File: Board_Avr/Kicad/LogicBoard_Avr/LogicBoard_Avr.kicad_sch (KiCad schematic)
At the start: 11 parts, among them SW1 Reset switch, U1 ATmega328PB-A

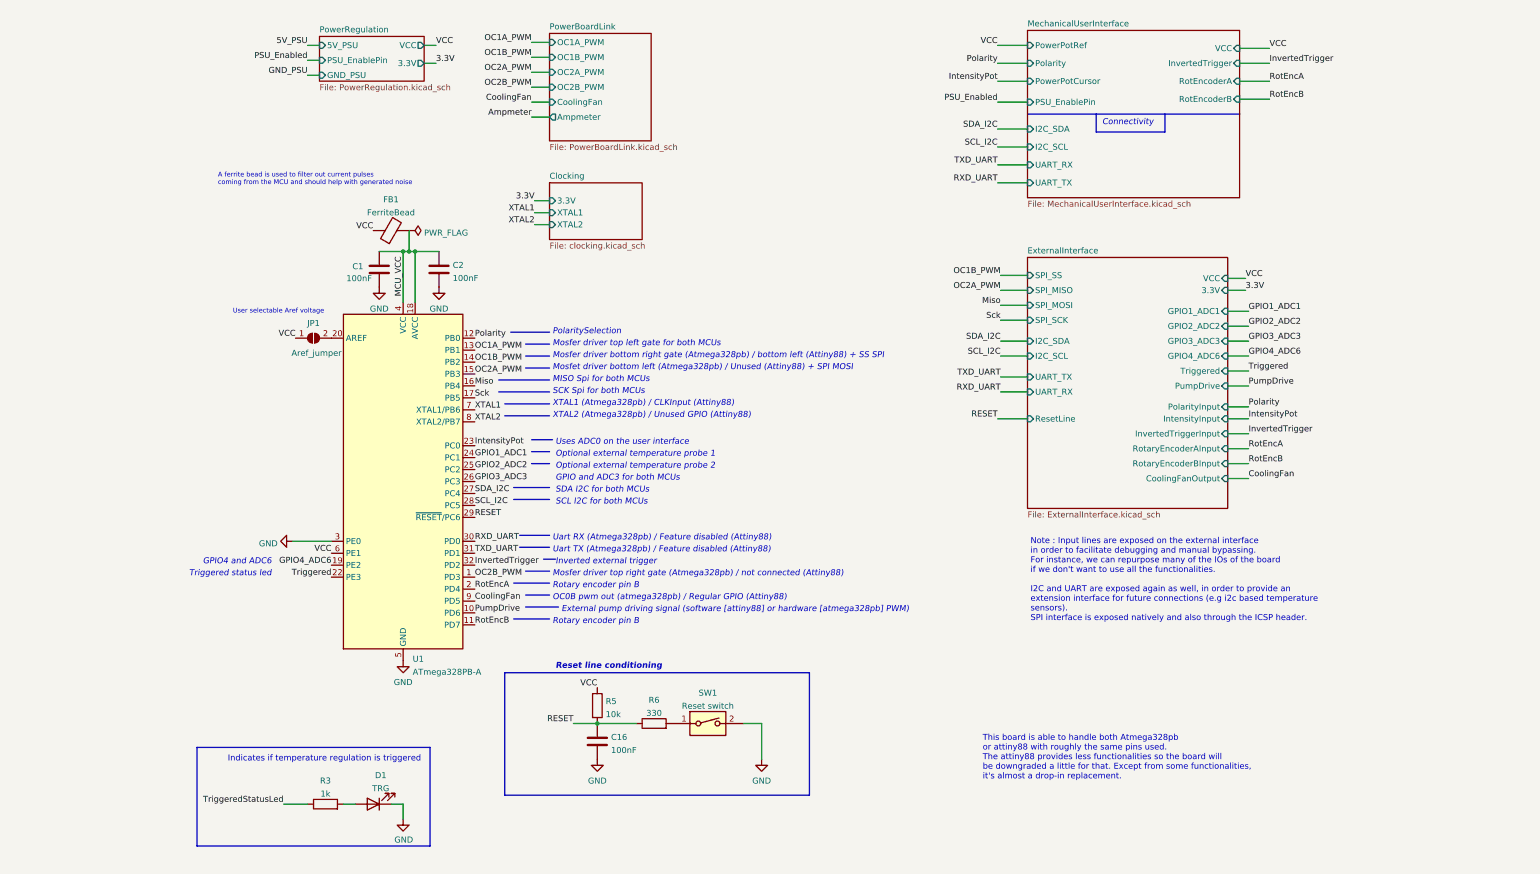
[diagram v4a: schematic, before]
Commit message: Fixed misorganised pins and updated pin mapping table
Signed-off-by: bebenlebricolo <benoittarrade@hotmail.fr>
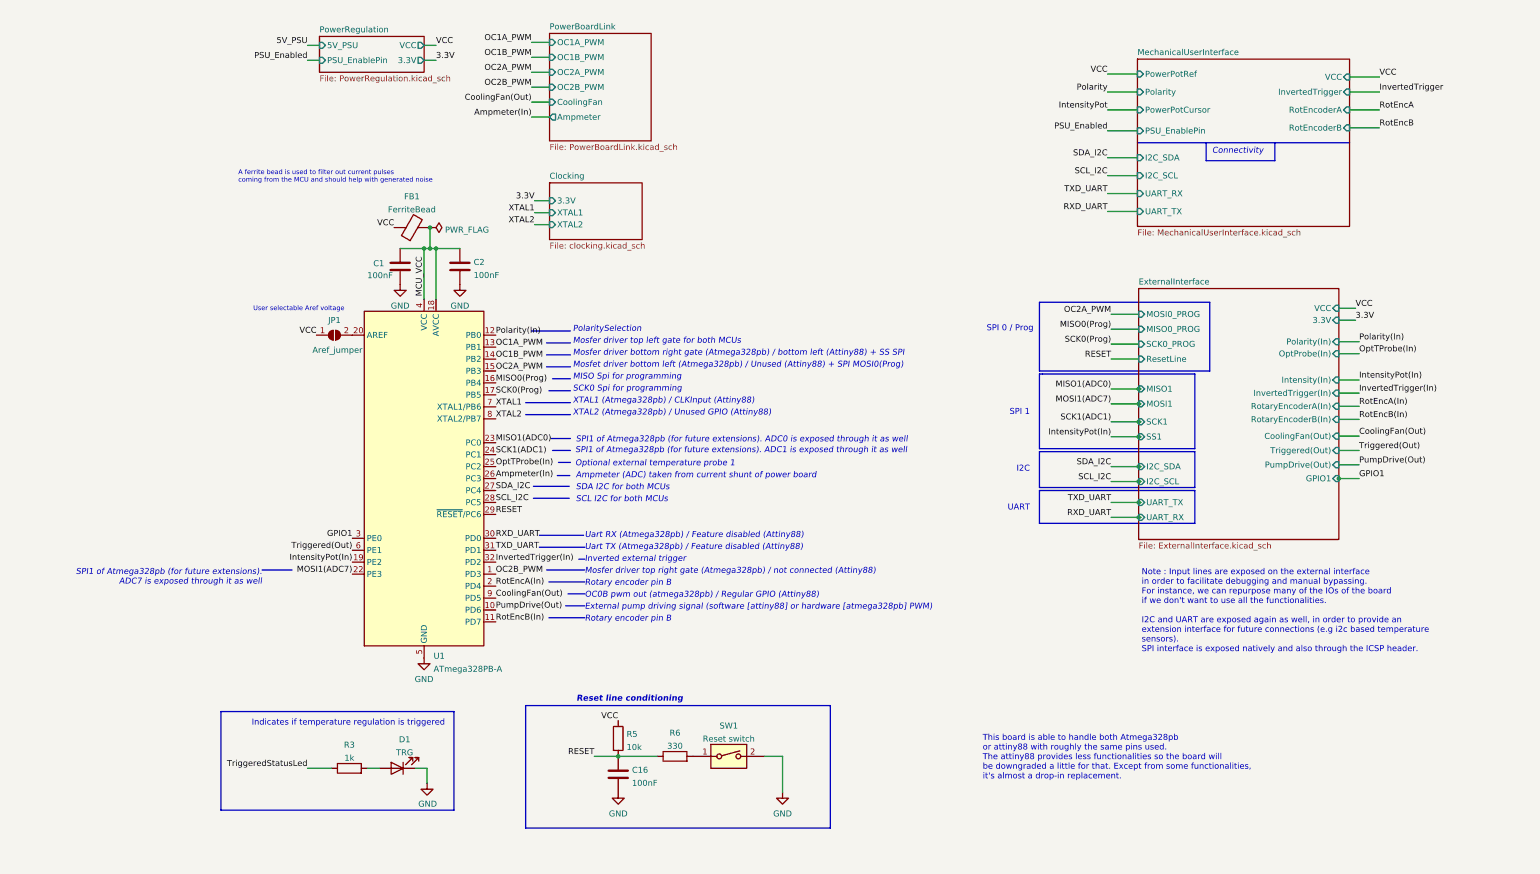
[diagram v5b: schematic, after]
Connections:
- net GND: no longer U1.3 (PE0)
- net IntensityPot: no longer U1.23 (PC0)
- net InvertedTrigger: no longer U1.32 (PD2)
- net Polarity: no longer U1.12 (PB0)
- net RotEncA: no longer U1.2 (PD4)
- net RotEncB: no longer U1.11 (PD7)
- net VCC: no longer U1.6 (PE1)
- net CoolingFan renamed CoolingFan(Out)
- net GPIO1_ADC1 renamed SCK1(ADC1)
- net GPIO2_ADC2 renamed OptTProbe(In)
- net GPIO3_ADC3 renamed Ampmeter(In)
- net GPIO4_ADC6 renamed IntensityPot(In)
- net Miso renamed MISO0(Prog)
- net PumpDrive renamed PumpDrive(Out)
- net Sck renamed SCK0(Prog)
- net Triggered renamed MOSI1(ADC7)
- new net GPIO1: U1.3 (PE0)
- new net InvertedTrigger(In): U1.32 (PD2)
- new net MISO1(ADC0): U1.23 (PC0)
- new net Polarity(In): U1.12 (PB0)
- new net RotEncA(In): U1.2 (PD4)
- new net RotEncB(In): U1.11 (PD7)
- new net Triggered(Out): U1.6 (PE1)
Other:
- sheet ExternalInterface ports: added CoolingFan(Out), GPIO1, Intensity(In), InvertedTrigger(In), MISO0_PROG, MISO1, MOSI0_PROG, MOSI1, OptProbe(In), Polarity(In), PumpDrive(Out), RotaryEncoderA(In), RotaryEncoderB(In), SCK0_PROG, SCK1, SS1, Triggered(Out); removed CoolingFanOutput, GPIO1_ADC1, GPIO2_ADC2, GPIO3_ADC3, GPIO4_ADC6, IntensityInput, InvertedTriggerInput, PolarityInput, PumpDrive, RotaryEncoderAInput, RotaryEncoderBInput, SPI_MISO, SPI_MOSI, SPI_SCK, SPI_SS, Triggered
- sheet PowerRegulation ports: added none; removed GND_PSU
- note added: "Ampmeter (ADC) taken from current shunt of power board"
- note added: "I2C"
- note added: "MISO Spi for programming"
- note added: "Mosfet driver bottom left (Atmega328pb) / Unused (Attiny88) + SPI MOSI0(Prog)"
- note added: "SCK0 Spi for programming"
- note added: "SPI 0 / Prog"
- note added: "SPI 1"
- note added: "SPI1 of Atmega328pb (for future extensions). ADC0 is exposed through it as well"
- note added: "SPI1 of Atmega328pb (for future extensions). ADC1 is exposed through it as well"
- note added: "SPI1 of Atmega328pb (for future extensions). ADC7 is exposed through it as well"
- note added: "UART"
- note removed: "GPIO and ADC3 for both MCUs"
- note removed: "GPIO4 and ADC6"
- note removed: "MISO Spi for both MCUs"
- note removed: "Mosfet driver bottom left (Atmega328pb) / Unused (Attiny88) + SPI MOSI"
- note removed: "Optional external temperature probe 2"
- note removed: "SCK Spi for both MCUs"
- note removed: "Triggered status led"
- note removed: "Uses ADC0 on the user interface"
- moved on the sheet: C1, C16, C2, D1, FB1, JP1, R3, R5, R6, SW1, U1

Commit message: Started routing all traces
Signed-off-by: bebenlebricolo <benoittarrade@hotmail.fr>
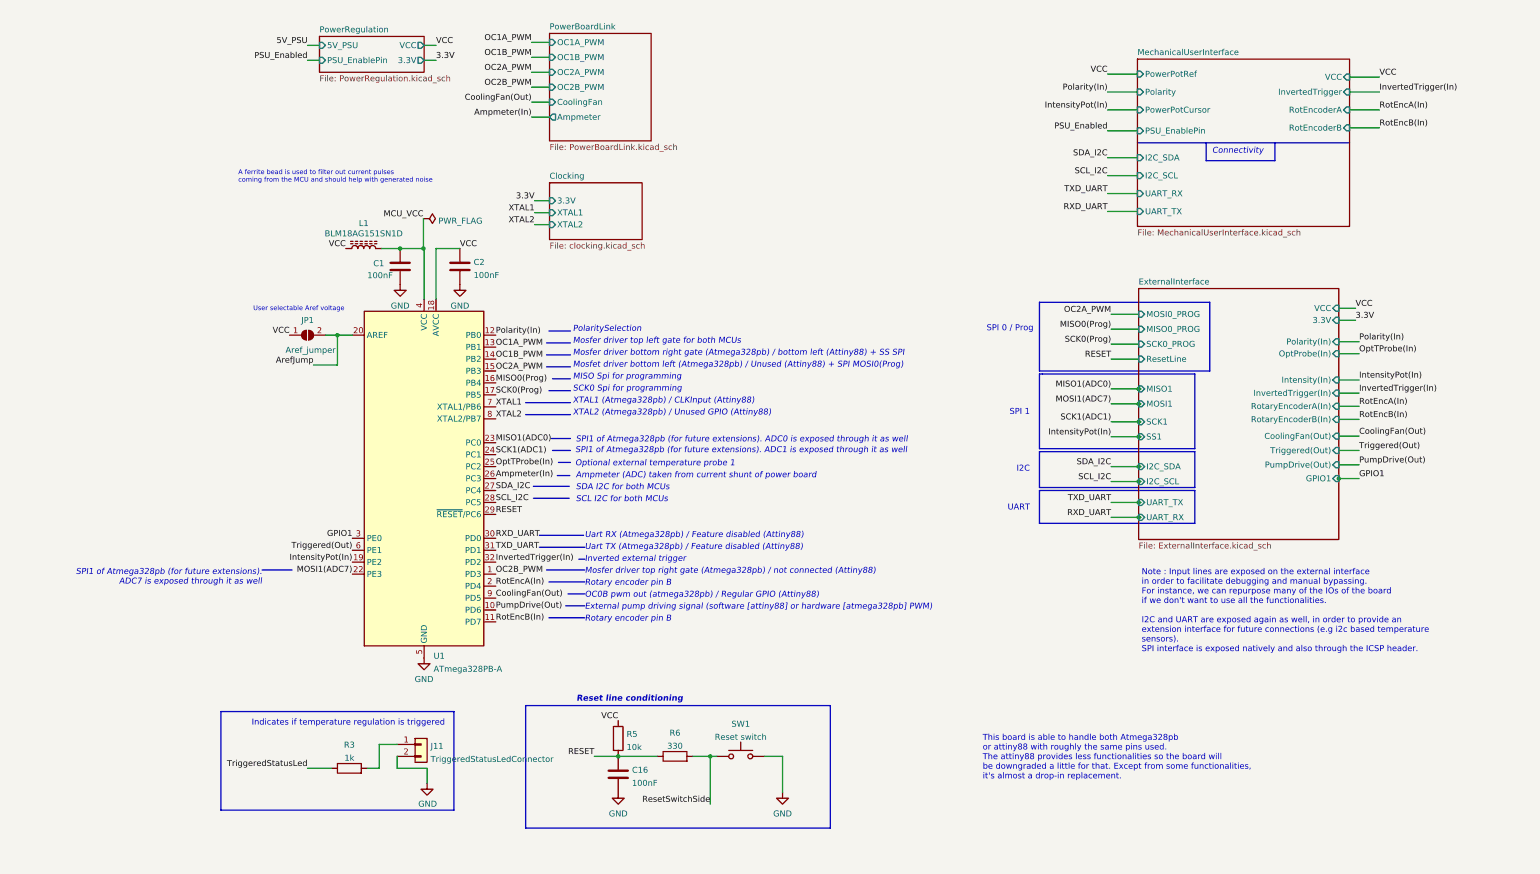
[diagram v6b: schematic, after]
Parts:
- removed D1: TRG, symbol Device:LED
- removed FB1: FerriteBead, symbol Device:FerriteBead
- removed SW1: Reset switch, symbol Switch:SW_DIP_x01
- added J11: TriggeredStatusLedConnector, Connector_PinHeader_2.54mm:PinHeader_1x02_P2.54mm_Vertical, symbol Connector_Generic:Conn_01x02
- added L1: BLM18AG151SN1D, Capacitor_SMD:C_0603_1608Metric, symbol Device:L_Ferrite
- added SW1: Reset switch, Button_Switch_THT:SW_PUSH_6mm_H4.3mm, symbol Switch:SW_Push
- C1, C16, C2: footprint (none) -> Capacitor_SMD:C_1206_3216Metric
- JP1: footprint (none) -> Jumper:SolderJumper-2_P1.3mm_Open_RoundedPad1.0x1.5mm
- R3, R5, R6: footprint (none) -> Resistor_SMD:R_1206_3216Metric_Pad1.30x1.75mm_HandSolder
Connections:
- net GND: now also J11.2 (Pin_2), SW1.2
- net MCU_VCC: now also L1.2; no longer C2.1, U1.18 (AVCC)
- net VCC: now also C2.1, U1.18 (AVCC), L1.1
- net at R3.2: now also J11.1 (Pin_1)
- net ArefJump: now reaches JP1.2 (B), U1.20 (AREF)
- net ResetSwitchSide: now reaches R6.2
- net ResetSwitchSide: now also SW1.1
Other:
- moved on the sheet: JP1

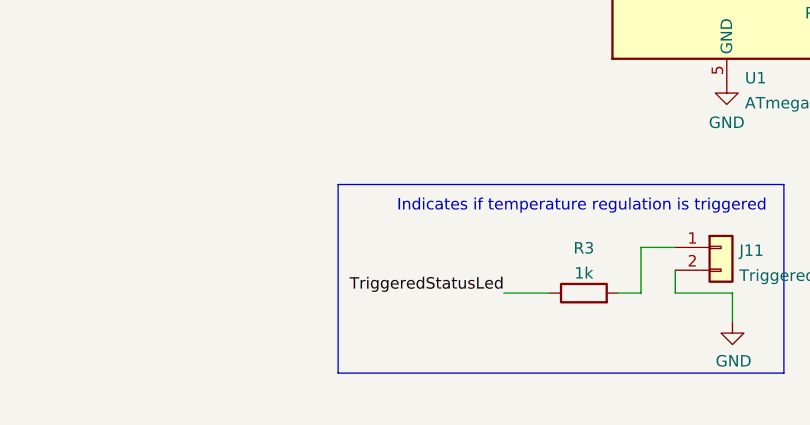
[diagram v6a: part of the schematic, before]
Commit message: Removed all microvias (unsupported by JLCPCB)
Signed-off-by: bebenlebricolo <benoittarrade@hotmail.fr>
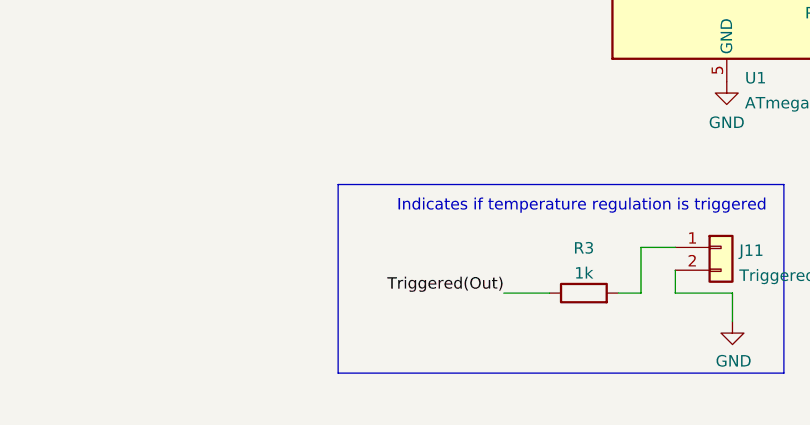
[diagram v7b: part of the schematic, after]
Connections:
- net TriggeredStatusLed is gone; now on net Triggered(Out): R3.1
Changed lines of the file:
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@@
     (effects (font (size 1.27 1.27)) (justify left bottom))
+  )
+  (label "Triggered(Out)" (at 36.83 175.26 180)
+    (effects (font (size 1.27 1.27)) (justify right bottom))
   )
   (label "Polarity(In)" (at 206.883 31.496 180)
@@
     (effects (font (size 1.27 1.27)) (justify left bottom))
   )
-  (label "TriggeredStatusLed" (at 36.83 175.26 180)
-    (effects (font (size 1.27 1.27)) (justify right bottom))
-  )
   (label "CoolingFan(Out)" (at 84.455 33.655 180)

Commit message: Finalised routing
Signed-off-by: bebenlebricolo <benoittarrade@hotmail.fr>
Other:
- sheet ExternalInterface ports: added none; removed I2C_SCL, I2C_SDA, UART_RX, UART_TX
- note removed: "I2C"
- note removed: "UART"
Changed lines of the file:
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@@
   (junction (at 122.428 172.72) (diameter 0) (color 0 0 0 0)
   )
-  (junction (at 213.487 111.125) (diameter 0) (color 0 0 0 0)
-  )
-  (junction (at 213.487 114.3) (diameter 0) (color 0 0 0 0)
-  )
   (junction (at 61.468 64.77) (diameter 0) (color 0 0 0 0)
   )
-  (junction (at 213.487 121.92) (diameter 0) (color 0 0 0 0)
-  )
   (junction (at 43.18 83.185) (diameter 0) (color 0 0 0 0)
   )
@@
   (junction (at 213.487 104.775) (diameter 0) (color 0 0 0 0)
   )
-  (junction (at 213.487 118.745) (diameter 0) (color 0 0 0 0)
-  )
   (junction (at 102.87 172.72) (diameter 0) (color 0 0 0 0)
   )
@@
     (stroke (width 0) (type default) (color 0 0 0 0))
   )
-  (polyline (pts (xy 192.405 107.95) (xy 225.425 107.95))
-    (stroke (width 0) (type default) (color 0 0 0 0))
-  )
   (wire (pts (xy 207.645 81.915) (xy 213.487 81.915))
     (stroke (width 0) (type default) (color 0 0 0 0))
@@
     (stroke (width 0) (type solid) (color 0 0 0 0))
   )
-  (wire (pts (xy 213.487 118.745) (xy 213.995 118.745))
-    (stroke (width 0) (type default) (color 0 0 0 0))
-  )
-  (wire (pts (xy 213.487 121.92) (xy 213.995 121.92))
-    (stroke (width 0) (type default) (color 0 0 0 0))
-  )
   (wire (pts (xy 256.032 107.696) (xy 260.35 107.696))
     (stroke (width 0) (type default) (color 0 0 0 0))
@@
     (stroke (width 0) (type default) (color 0 0 0 0))
   )
-  (polyline (pts (xy 225.425 115.57) (xy 192.405 115.57))
-    (stroke (width 0) (type default) (color 0 0 0 0))
-  )
   (polyline (pts (xy 242.443 46.101) (xy 242.443 42.291))
     (stroke (width 0) (type default) (color 0 0 0 0))
@@
     (stroke (width 0) (type default) (color 0 0 0 0))
   )
-  (polyline (pts (xy 192.405 107.95) (xy 192.405 115.57))
-    (stroke (width 0) (type default) (color 0 0 0 0))
-  )
   (wire (pts (xy 84.455 24.13) (xy 88.265 24.13))
     (stroke (width 0) (type default) (color 0 0 0 0))
@@
     (stroke (width 0) (type default) (color 0 0 0 0))
   )
-  (polyline (pts (xy 192.405 116.205) (xy 225.425 116.205))
-    (stroke (width 0) (type default) (color 0 0 0 0))
-  )
   (wire (pts (xy 207.645 104.775) (xy 213.487 104.775))
     (stroke (width 0) (type default) (color 0 0 0 0))
@@
     (stroke (width 0) (type default) (color 0 0 0 0))
   )
-  (polyline (pts (xy 192.405 116.205) (xy 192.405 123.19))
-    (stroke (width 0) (type default) (color 0 0 0 0))
-  )
   (wire (pts (xy 84.455 27.305) (xy 88.265 27.305))
     (stroke (width 0) (type default) (color 0 0 0 0))
@@
     (stroke (width 0) (type solid) (color 0 0 0 0))
   )
-  (wire (pts (xy 207.645 121.92) (xy 213.487 121.92))
-    (stroke (width 0) (type default) (color 0 0 0 0))
-  )
   (polyline (pts (xy 225.425 91.44) (xy 225.425 107.315))
     (stroke (width 0) (type default) (color 0 0 0 0))
@@
     (stroke (width 0) (type default) (color 0 0 0 0))
   )
-  (wire (pts (xy 207.645 118.745) (xy 213.487 118.745))
-    (stroke (width 0) (type default) (color 0 0 0 0))
-  )
   (wire (pts (xy 55.88 175.26) (xy 62.23 175.26))
     (stroke (width 0) (type default) (color 0 0 0 0))
@@
     (stroke (width 0) (type default) (color 0 0 0 0))
   )
-  (polyline (pts (xy 225.425 107.95) (xy 225.425 115.57))
-    (stroke (width 0) (type default) (color 0 0 0 0))
-  )
   (wire (pts (xy 213.233 56.896) (xy 206.883 56.896))
     (stroke (width 0) (type default) (color 0 0 0 0))
@@
     (stroke (width 0) (type default) (color 0 0 0 0))
   )
-  (wire (pts (xy 213.487 111.125) (xy 213.995 111.125))
-    (stroke (width 0) (type default) (color 0 0 0 0))
-  )
-  (polyline (pts (xy 225.425 123.19) (xy 192.405 123.19))
-    (stroke (width 0) (type default) (color 0 0 0 0))
-  )
-  (wire (pts (xy 213.487 114.3) (xy 213.995 114.3))
-    (stroke (width 0) (type default) (color 0 0 0 0))
-  )
   (wire (pts (xy 213.487 101.6) (xy 213.995 101.6))
     (stroke (width 0) (type default) (color 0 0 0 0))
@@
     (stroke (width 0) (type default) (color 0 0 0 0))
   )
-  (wire (pts (xy 207.645 111.125) (xy 213.487 111.125))
-    (stroke (width 0) (type default) (color 0 0 0 0))
-  )
   (wire (pts (xy 256.032 80.01) (xy 259.588 80.01))
     (stroke (width 0) (type default) (color 0 0 0 0))
@@
     (stroke (width 0) (type default) (color 0 0 0 0))
   )
-  (wire (pts (xy 207.645 114.3) (xy 213.487 114.3))
-    (stroke (width 0) (type default) (color 0 0 0 0))
-  )
   (wire (pts (xy 256.032 98.298) (xy 260.35 98.298))
     (stroke (width 0) (type default) (color 0 0 0 0))
@@
   )
   (wire (pts (xy 84.455 30.48) (xy 88.265 30.48))
-    (stroke (width 0) (type default) (color 0 0 0 0))
-  )
-  (polyline (pts (xy 225.425 116.205) (xy 225.425 123.19))
     (stroke (width 0) (type default) (color 0 0 0 0))
   )
@@
     (effects (font (size 1.27 1.27) italic) (justify right bottom))
   )
-  (text "UART" (at 190.373 120.65 180)
-    (effects (font (size 1.27 1.27)) (justify right bottom))
-  )
   (text "Rotary encoder pin B" (at 95.758 144.272 0)
     (effects (font (size 1.27 1.27) italic) (justify left bottom))
@@
   (text "Inverted external trigger " (at 95.758 131.572 0)
     (effects (font (size 1.27 1.27) italic) (justify left bottom))
-  )
-  (text "I2C " (at 190.373 112.395 180)
-    (effects (font (size 1.27 1.27)) (justify right bottom))
   )
   (text "Connectivity" (at 229.108 44.831 0)
@@
     (effects (font (size 1.27 1.27)) (justify left bottom))
   )
-  (label "TXD_UART" (at 207.645 118.745 180)
-    (effects (font (size 1.27 1.27)) (justify right bottom))
-  )
   (label "IntensityPot(In)" (at 207.645 104.775 180)
     (effects (font (size 1.27 1.27)) (justify right bottom))
@@
     (effects (font (size 1.27 1.27)) (justify right bottom))
   )
-  (label "RXD_UART" (at 207.645 121.92 180)
-    (effects (font (size 1.27 1.27)) (justify right bottom))
-  )
   (label "XTAL1" (at 85.09 57.15 180)
     (effects (font (size 1.27 1.27)) (justify right bottom))
@@
     (effects (font (size 1.27 1.27)) (justify right bottom))
   )
-  (label "SCL_I2C" (at 207.645 114.3 180)
-    (effects (font (size 1.27 1.27)) (justify right bottom))
-  )
   (label "OC2A_PWM" (at 207.645 78.74 180)
     (effects (font (size 1.27 1.27)) (justify right bottom))
@@
   (label "VCC" (at 264.668 28.321 0)
     (effects (font (size 1.27 1.27)) (justify left bottom))
-  )
-  (label "SDA_I2C" (at 207.645 111.125 180)
-    (effects (font (size 1.27 1.27)) (justify right bottom))
   )
   (label "SCK0(Prog)" (at 76.835 95.885 0)
@@
       (effects (font (size 1.27 1.27)) (justify left top))
     )
-    (pin "I2C_SDA" input (at 213.487 111.125 180)
-      (effects (font (size 1.27 1.27)) (justify left))
-    )
-    (pin "I2C_SCL" input (at 213.487 114.3 180)
-      (effects (font (size 1.27 1.27)) (justify left))
-    )
-    (pin "UART_TX" input (at 213.487 118.745 180)
-      (effects (font (size 1.27 1.27)) (justify left))
-    )
-    (pin "UART_RX" input (at 213.487 121.92 180)
-      (effects (font (size 1.27 1.27)) (justify left))
-    )
     (pin "VCC" input (at 256.032 77.47 0)
       (effects (font (size 1.27 1.27)) (justify right))
@@
       (reference "R6") (unit 1) (value "330") (footprint "Resistor_SMD:R_1206_3216Metric_Pad1.30x1.75mm_HandSolder")
     )
+    (path "/f7bab2a7-6dbd-496a-8aa4-c4dda7ee3f09/5d7592ea-ef51-4262-a6ff-7bf9ba2d179e"
+      (reference "R7") (unit 1) (value "33") (footprint "Resistor_SMD:R_0402_1005Metric_Pad0.72x0.64mm_HandSolder")
+    )
+    (path "/f7bab2a7-6dbd-496a-8aa4-c4dda7ee3f09/5b6c2f76-1795-4111-8161-cf6c2a83b363"
+      (reference "R8") (unit 1) (value "33") (footprint "Resistor_SMD:R_0402_1005Metric_Pad0.72x0.64mm_HandSolder")
+    )
+    (path "/f7bab2a7-6dbd-496a-8aa4-c4dda7ee3f09/f7770c87-2577-4a8a-9fb0-515b4cfc5e20"
+      (reference "R9") (unit 1) (value "33") (footprint "Resistor_SMD:R_0402_1005Metric_Pad0.72x0.64mm_HandSolder")
+    )
+    (path "/f7bab2a7-6dbd-496a-8aa4-c4dda7ee3f09/d64799db-c254-46c6-97ca-53ff1c854419"
+      (reference "R10") (unit 1) (value "33") (footprint "Resistor_SMD:R_0402_1005Metric_Pad0.72x0.64mm_HandSolder")
+    )
     (path "/b2a07428-2d70-4877-bb9f-f602752b7d1e"
